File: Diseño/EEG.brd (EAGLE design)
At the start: 100 x 80 mm, 34 parts, among them IC1 REF2033AIDDCT, IC2 MCP73831T-2ACI_OT, IC3 LP38692MP-3.3_NOPB, J1 USB3500-30-A-KIT, J2 SJ3-35083A-TR

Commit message: Se actualizó la esp32-s3
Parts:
- added R3: 1.5K, rcl:R0805
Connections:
- new net RX: ESP32-S3.36
- new net TOUCHP_1: ESP32-S3.17
- new net TOUCHP_2: ESP32-S3.18
- new net TOUCHP_3: ESP32-S3.19
- new net TX: ESP32-S3.37
- new net USB_2: ESP32-S3.13, J1.2
- new net USB_3: ESP32-S3.14, J1.3, R3.2
- net +3V3: now also R3.1
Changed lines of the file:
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@@
 <attribute name="VALUE" x="0" y="-25.4" size="1.27" layer="27"/>
+</element>
+<element name="R3" library="rcl" library_urn="urn:adsk.eagle:library:334" package="R0805" package3d_urn="urn:adsk.eagle:package:23553/2" value="1.5K" x="1.27" y="-29.21" smashed="yes">
+<attribute name="NAME" x="0.635" y="-27.94" size="1.27" layer="25"/>
+<attribute name="POPULARITY" value="86" x="1.27" y="-29.21" size="1.778" layer="27" display="off"/>
+<attribute name="SPICEPREFIX" value="R" x="1.27" y="-29.21" size="1.778" layer="27" display="off"/>
+<attribute name="VALUE" x="0.635" y="-31.75" size="1.27" layer="27"/>
 </element>
 </elements>
@@
 <contactref element="HIGH_PASS_1" pad="5"/>
 <contactref element="LOW_PASS_1" pad="5"/>
-<wire x1="27.285" y1="41.595" x2="28.555" y2="37.78" width="0" layer="19" extent="1-1"/>
+<contactref element="R3" pad="1"/>
+<wire x1="51.115" y1="53.34" x2="78.88" y2="68.76" width="0" layer="19" extent="1-1"/>
+<wire x1="47.945" y1="60.325" x2="51.115" y2="53.34" width="0" layer="19" extent="1-1"/>
+<wire x1="40.955" y1="46.99" x2="51.115" y2="53.34" width="0" layer="19" extent="1-1"/>
+<wire x1="27.285" y1="49.845" x2="40.955" y2="46.99" width="0" layer="19" extent="1-1"/>
+<wire x1="27.285" y1="41.595" x2="27.285" y2="49.845" width="0" layer="19" extent="1-1"/>
 <wire x1="24.785" y1="41.595" x2="27.285" y2="41.595" width="0" layer="19" extent="1-1"/>
-<wire x1="27.285" y1="49.845" x2="24.785" y2="41.595" width="0" layer="19" extent="1-1"/>
-<wire x1="10.332" y1="69.215" x2="27.285" y2="49.845" width="0" layer="19" extent="1-1"/>
-<wire x1="47.945" y1="60.325" x2="10.332" y2="69.215" width="0" layer="19" extent="1-1"/>
-<wire x1="51.115" y1="53.34" x2="47.945" y2="60.325" width="0" layer="19" extent="1-1"/>
-<wire x1="40.955" y1="46.99" x2="51.115" y2="53.34" width="0" layer="19" extent="1-1"/>
-<wire x1="8.38" y1="47.51" x2="40.955" y2="46.99" width="0" layer="19" extent="1-1"/>
-<wire x1="9.505" y1="61.275" x2="27.285" y2="49.845" width="0" layer="19" extent="1-1"/>
-<wire x1="78.88" y1="68.76" x2="8.38" y2="47.51" width="0" layer="19" extent="1-1"/>
+<wire x1="28.555" y1="37.78" x2="27.285" y2="41.595" width="0" layer="19" extent="1-1"/>
+<wire x1="8.38" y1="47.51" x2="24.785" y2="41.595" width="0" layer="19" extent="1-1"/>
+<wire x1="9.505" y1="61.275" x2="8.38" y2="47.51" width="0" layer="19" extent="1-1"/>
+<wire x1="10.332" y1="69.215" x2="9.505" y2="61.275" width="0" layer="19" extent="1-1"/>
+<wire x1="0.32" y1="-29.21" x2="28.555" y2="37.78" width="0" layer="19" extent="1-1"/>
 </signal>
 <signal name="GND">
@@
 <wire x1="2.22" y1="-22.86" x2="14.58" y2="38.73" width="0" layer="19" extent="1-1"/>
 </signal>
+<signal name="USB_2">
+<contactref element="J1" pad="2"/>
+<contactref element="ESP32-S3" pad="13"/>
+<wire x1="6.335" y1="-1.915" x2="78.88" y2="54.79" width="0" layer="19" extent="1-1"/>
+</signal>
+<signal name="USB_3">
+<contactref element="J1" pad="3"/>
+<contactref element="ESP32-S3" pad="14"/>
+<contactref element="R3" pad="2"/>
+<wire x1="6.985" y1="-1.915" x2="78.88" y2="53.52" width="0" layer="19" extent="1-1"/>
+<wire x1="2.22" y1="-29.21" x2="6.985" y2="-1.915" width="0" layer="19" extent="1-1"/>
+</signal>
+<signal name="RX">
+<contactref element="ESP32-S3" pad="36"/>
+</signal>
+<signal name="TX">
+<contactref element="ESP32-S3" pad="37"/>
+</signal>
+<signal name="TOUCHP_2">
+<contactref element="ESP32-S3" pad="18"/>
+</signal>
+<signal name="TOUCHP_3">
+<contactref element="ESP32-S3" pad="19"/>
+</signal>
+<signal name="TOUCHP_1">
+<contactref element="ESP32-S3" pad="17"/>
+</signal>
 </signals>

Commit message: Correcion de conexiones, añadido leds indicadores de estados FSM
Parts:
- added LED_CAPTURA, LED_PROCESAMIENTO, LED_REPOSO, LED_RESULTADO: (no value), led:CHIPLED_0805
- added R4: 220, rcl:R0805
- moved C4 118.2 mm to (68.6, 74.3)
- moved R3 118.2 mm to (68.6, 67.9)
- moved J1 47.4 mm to (47.0, 19.7)
- moved J2 47.4 mm to (45.1, 8.89)
- renumbered LED1 to LED_CARGA
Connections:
- new net +5V1: ESP32-S3.22
- new net LED_REP: ESP32-S3.21, LED_REPOSO.A
- new net N$1: ESP32-S3.5, LED_CAPTURA.A
- new net N$15: LED_CAPTURA.C, LED_PROCESAMIENTO.C, LED_REPOSO.C, LED_RESULTADO.C, R4.2
- new net N$16: ESP32-S3.6, LED_PROCESAMIENTO.A
- new net N$17: ESP32-S3.7, LED_RESULTADO.A
- net GND: now also R4.1

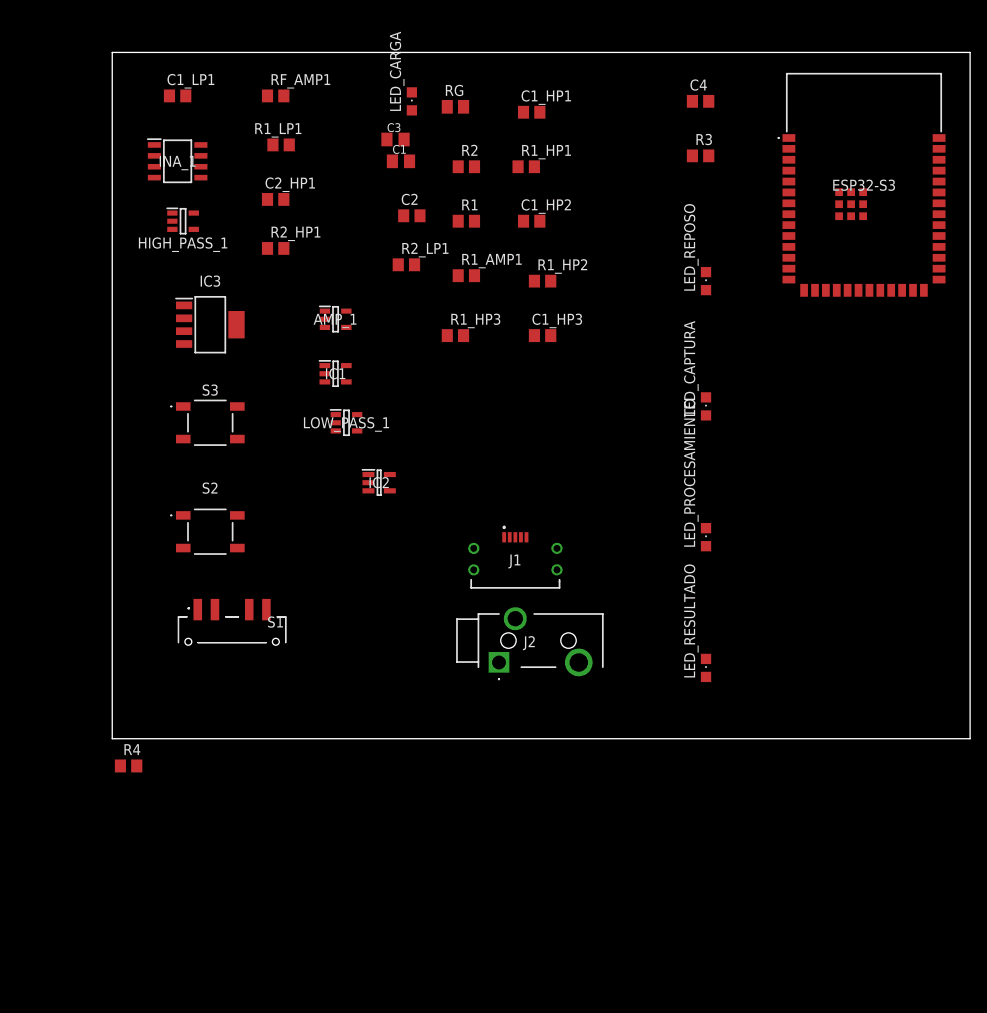
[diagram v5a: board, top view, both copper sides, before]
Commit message: Se cambiaron alguno nombres para evitar confusiones
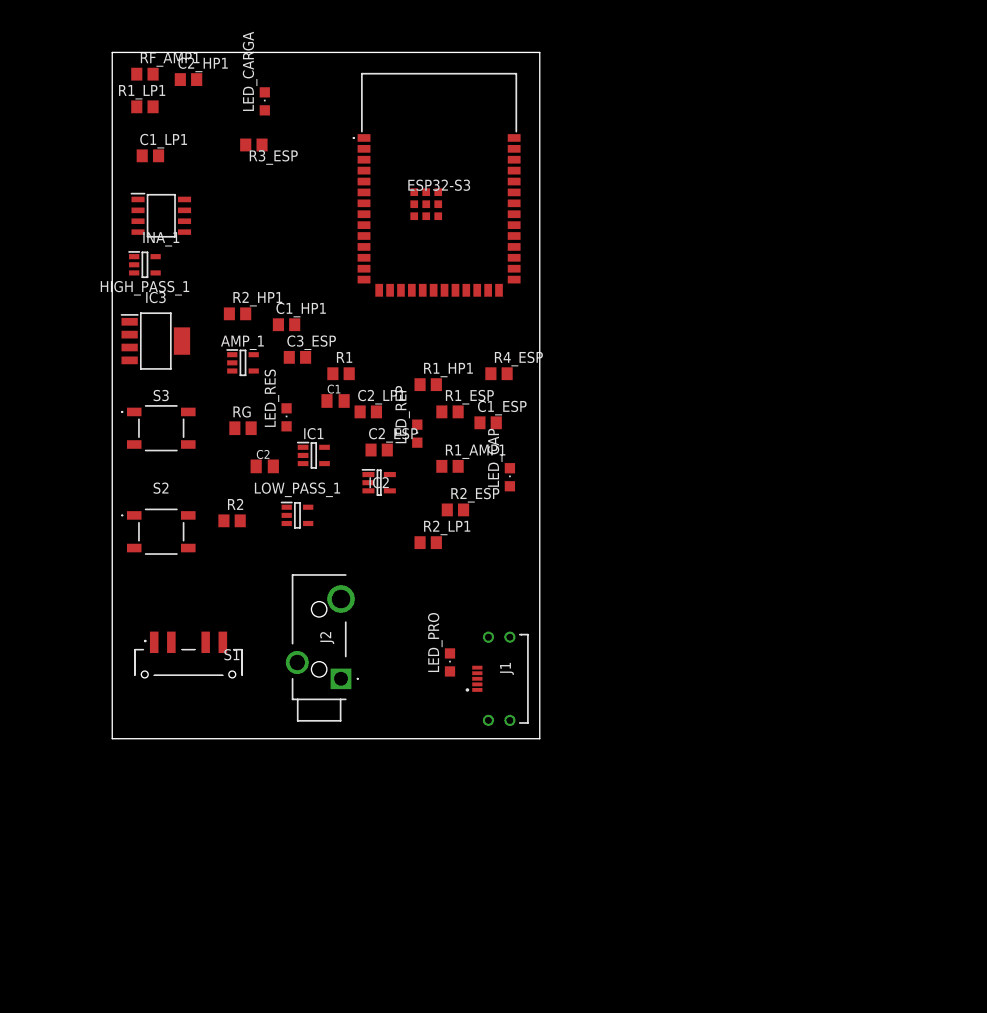
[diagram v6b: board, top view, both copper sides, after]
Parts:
- removed C1_HP2, C1_HP3: 0.1uF, rcl:C0805
- removed C3: (no value), rcl:C0805K
- removed C4: 0.1 uF, rcl:C0805
- removed LED_CAPTURA, LED_PROCESAMIENTO, LED_REPOSO, LED_RESULTADO: (no value), led:CHIPLED_0805
- removed R1_HP2, R1_HP3: 10k, rcl:R0805
- removed R3: 1.5K, rcl:R0805
- removed R4: 220, rcl:R0805
- added C1_ESP, C2_ESP: 0.1uF, rcl:C0805
- added C2_LP1: 100nF, rcl:C0805
- added C3_ESP: 0.1 uF, rcl:C0805
- added LED_CAP, LED_PRO, LED_REP, LED_RES: (no value), led:CHIPLED_0805
- added R1_ESP, R4_ESP: 10k, rcl:R0805
- added R2_ESP: 220, rcl:R0805
- added R3_ESP: 1.5K, rcl:R0805
- C2: value 100nF -> (none); device rcl:C0805 -> rcl:C0805K
- moved ESP32-S3 49.5 mm to (38.1, 64.8)
- moved R2 49.5 mm to (14.0, 25.4)
- moved RG 44.9 mm to (15.2, 36.2)
- moved C1_HP1 37.8 mm to (20.3, 48.3)
- moved C2 33.9 mm to (17.8, 31.8)
- moved R2_LP1 32.5 mm to (36.8, 22.9)
- moved C1 29.0 mm to (26.0, 39.4)
- moved R1_HP1 27.9 mm to (36.8, 41.3)
- moved R1 23.0 mm to (26.7, 42.5)
- moved R1_AMP1 22.3 mm to (39.4, 31.8)
- moved J2 18.5 mm to (26.7, 6.99), turned to 90 degrees
- moved C2_HP1 17.3 mm to (8.89, 76.8)
- moved LED_CARGA 17.1 mm to (17.8, 74.3)
- moved R1_LP1 16.5 mm to (3.81, 73.7)
- moved RF_AMP1 15.5 mm to (3.81, 77.5)
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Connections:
- net +3V3: now also C2_ESP.1, R1_ESP.2, R3_ESP.1, R4_ESP.2; no longer C1_HP2.1, R1_HP2.2, R1_HP3.2, R3.1
- net +5V: now also C2.1; no longer C3.1
- net GND: now also C1_ESP.1, C2.2, C2_ESP.2, C3_ESP.1, R2_ESP.1; no longer C1_HP2.2, C1_HP3.1, C3.2, C4.1, R4.1
- net LED_REP: now also LED_REP.A; no longer LED_REPOSO.A
- net N$1: now also LED_CAP.A; no longer LED_CAPTURA.A
- net N$13: now also C3_ESP.2, R4_ESP.1; no longer C4.2, R1_HP3.1
- net N$15: now also LED_CAP.C, LED_PRO.C, LED_REP.C, LED_RES.C, R2_ESP.2; no longer LED_CAPTURA.C, LED_PROCESAMIENTO.C, LED_REPOSO.C, LED_RESULTADO.C, R4.2
- net N$16: now also LED_PRO.A; no longer LED_PROCESAMIENTO.A
- net N$17: now also LED_RES.A; no longer LED_RESULTADO.A
- net N$19: now also C1_ESP.2, R1_ESP.1; no longer C1_HP3.2, R1_HP2.1
- net N$7: now also C2_LP1.1; no longer C2.1
- net USB_3: now also R3_ESP.2; no longer R3.2
- net VSS: now also C2_LP1.2; no longer C2.2
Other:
- board size 100 x 80 mm -> 49.8 x 80 mm

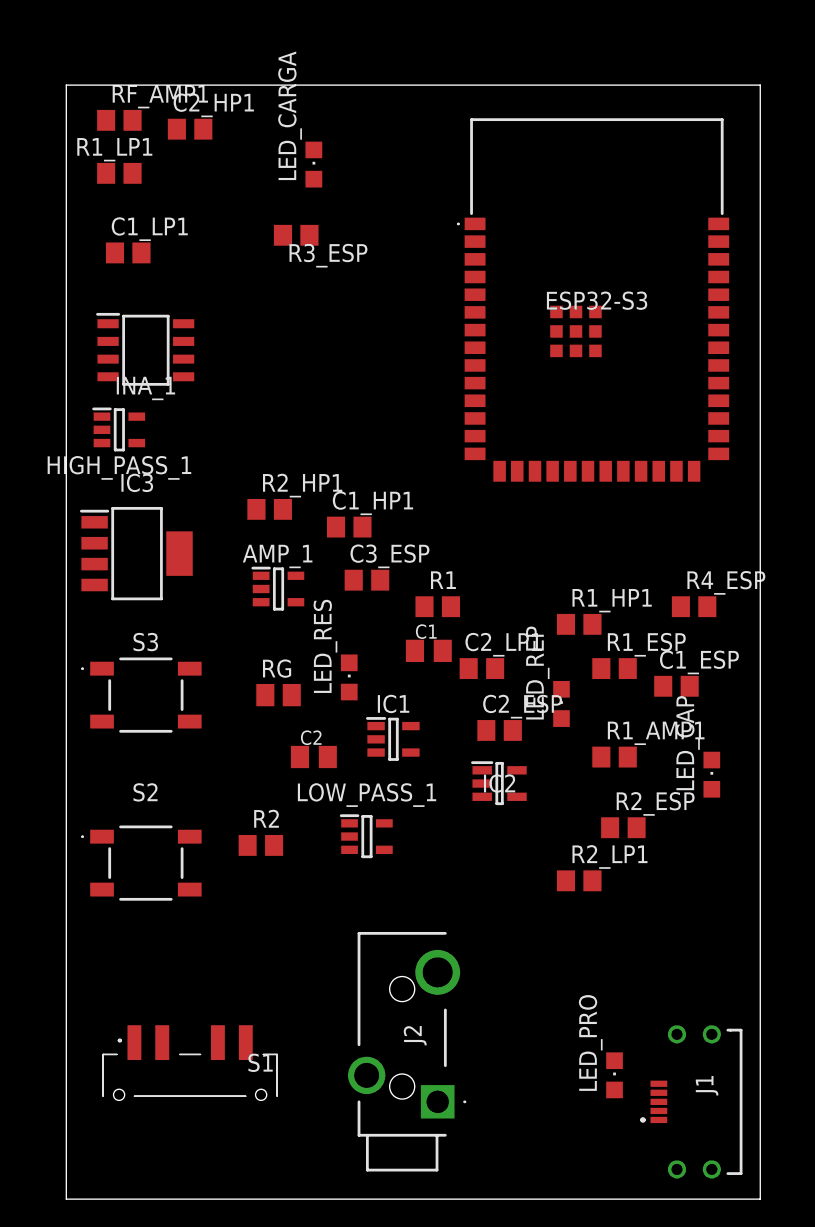
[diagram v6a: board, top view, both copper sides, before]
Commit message: Se adelantó la PCB separando los componentes por secciones de potencia, analógica y digital
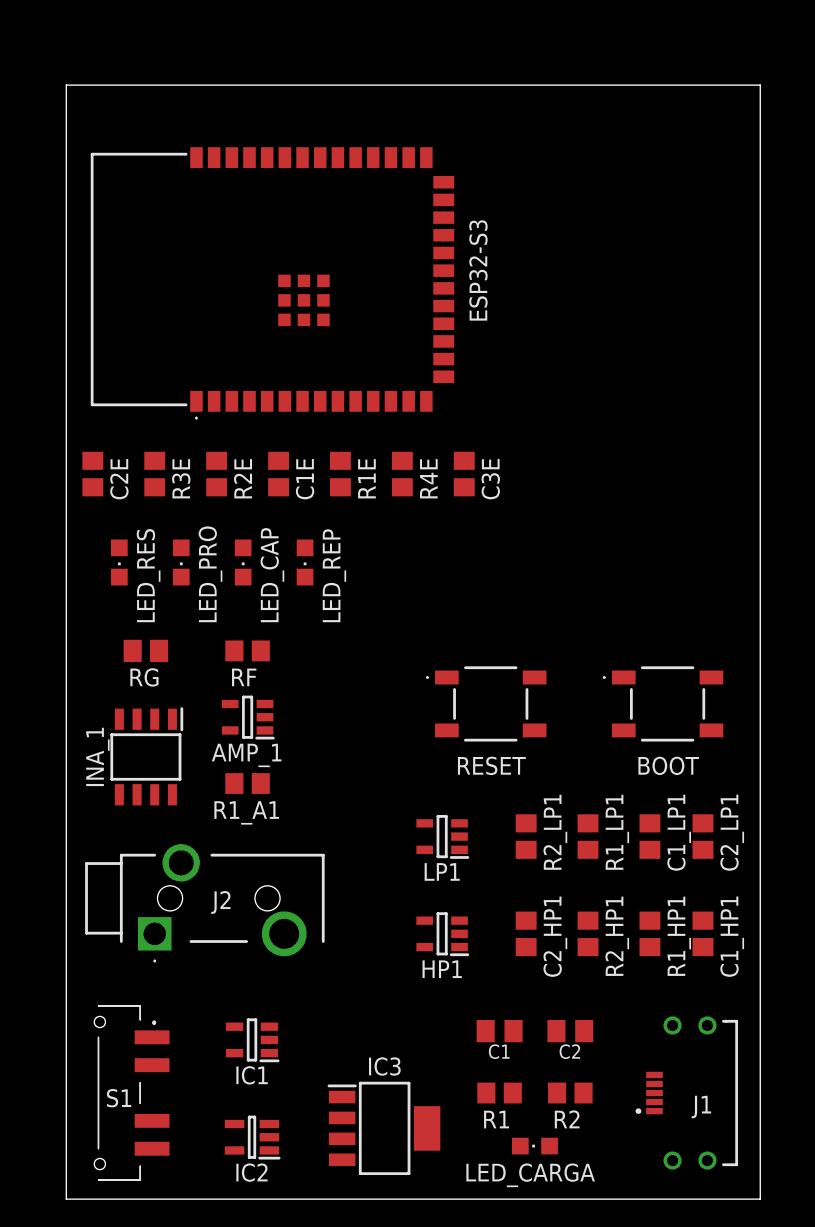
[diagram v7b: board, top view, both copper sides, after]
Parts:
- removed C1_ESP, C2_ESP: 0.1uF, rcl:C0805
- removed C3_ESP: 0.1 uF, rcl:C0805
- removed HIGH_PASS_1, LOW_PASS_1: LMV321AUIDBVR, LMV321AUIDBVR:SOT95P280X145-5N
- removed R1_AMP1: 1k, rcl:R0805
- removed R1_ESP, R4_ESP: 10k, rcl:R0805
- removed R2_ESP: 220, rcl:R0805
- removed R3_ESP: 1.5K, rcl:R0805
- removed RF_AMP1: 51k, rcl:R0805
- removed S2, S3: TS18-5-17-SL-160-SMT-TR, TS18-5-17-SL-160-SMT-TR:TS18517SL160SMTTR
- added BOOT, RESET: TS18-5-17-SL-160-SMT-TR, TS18-5-17-SL-160-SMT-TR:TS18517SL160SMTTR
- added C1E, C2E: 0.1uF, rcl:C0805
- added C3E: 0.1 uF, rcl:C0805
- added HP1, LP1: LMV321AUIDBVR, LMV321AUIDBVR:SOT95P280X145-5N
- added R1E, R4E: 10k, rcl:R0805
- added R1_A1: 1k, rcl:R0805
- added R2E: 220, rcl:R0805
- added R3E: 1.5K, rcl:R0805
- added RF: 51k, rcl:R0805
- moved LED_CARGA 72.3 mm to (33.7, 3.81), turned to 90 degrees
- moved C2_HP1 62.6 mm to (33.0, 19.1), turned to 90 degrees
- moved R1_LP1 58.3 mm to (37.5, 26.0), turned to 90 degrees
- moved C1_LP1 56.2 mm to (41.9, 26.0), turned to 270 degrees
- moved LED_PRO 48.2 mm to (8.26, 45.7), turned to 180 degrees
- moved IC3 44.9 mm to (22.9, 5.08)
- moved C1_HP1 38.7 mm to (45.7, 19.1), turned to 270 degrees
- moved R2_HP1 38.1 mm to (37.5, 19.1), turned to 90 degrees
- moved LED_CAP 36.9 mm to (12.7, 45.7), turned to 180 degrees
- moved R1 35.2 mm to (31.1, 7.62)
- moved IC2 31.0 mm to (13.3, 4.45), turned to 180 degrees
- moved INA_1 29.2 mm to (5.71, 31.8), turned to 270 degrees
- moved R2 28.5 mm to (36.2, 7.62), turned to 180 degrees
- moved C1 27.8 mm to (31.1, 12.1), turned to 180 degrees
- moved C2 27.0 mm to (36.2, 12.1)
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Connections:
- net +3V3: now also C2E.1, HP1.5, LP1.5, R1E.2, R3E.1, R4E.2; no longer C2_ESP.1, HIGH_PASS_1.5, LOW_PASS_1.5, R1_ESP.2, R3_ESP.1, R4_ESP.2
- net GND: now also BOOT.4, C1E.1, C2E.2, C3E.1, HP1.2, LP1.2, R2E.1, RESET.3; no longer C1_ESP.1, C2_ESP.2, C3_ESP.1, HIGH_PASS_1.2, LOW_PASS_1.2, R2_ESP.1, S2.3, S3.4
- net N$13: now also BOOT.2, C3E.2, R4E.1; no longer C3_ESP.2, R4_ESP.1, S3.2
- net N$15: now also R2E.2; no longer R2_ESP.2
- net N$19: now also C1E.2, R1E.1, RESET.1; no longer C1_ESP.2, R1_ESP.1, S2.1
- net N$5: now also HP1.1; no longer HIGH_PASS_1.1
- net N$7: now also LP1.1; no longer LOW_PASS_1.1
- net N$8: now also R1_A1.2, RF.1; no longer R1_AMP1.2, RF_AMP1.1
- net O2: now also HP1.3, HP1.4; no longer HIGH_PASS_1.3, HIGH_PASS_1.4
- net O3: now also LP1.3, LP1.4, R1_A1.1; no longer LOW_PASS_1.3, LOW_PASS_1.4, R1_AMP1.1
- net O4: now also RF.2; no longer RF_AMP1.2
- net USB_3: now also R3E.2; no longer R3_ESP.2

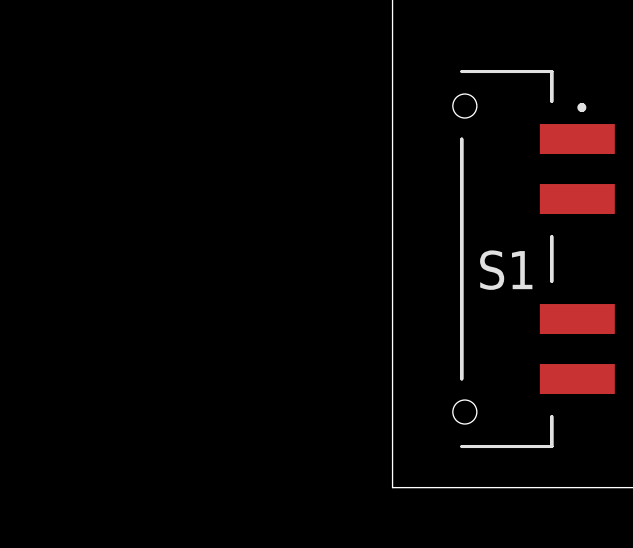
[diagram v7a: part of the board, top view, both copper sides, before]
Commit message: añadí el conector de la bateria
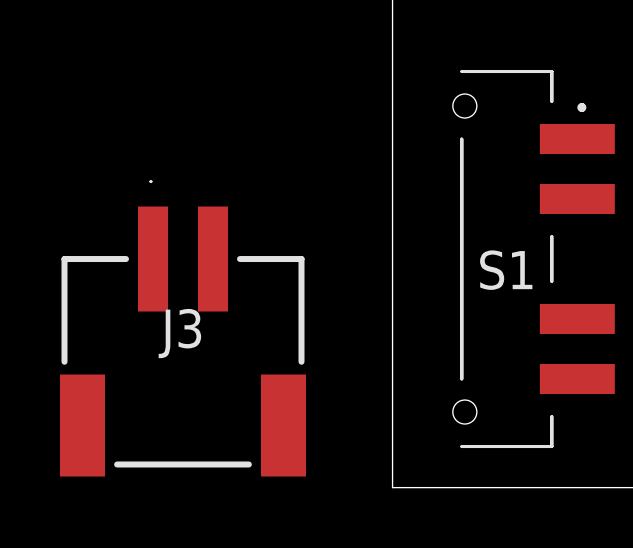
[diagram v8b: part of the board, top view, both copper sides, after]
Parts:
- added J3: 1769, 1769 (1):1769
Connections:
- net +5V: now also J3.3
- net GND: now also J3.4
